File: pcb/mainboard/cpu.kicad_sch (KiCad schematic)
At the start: 25 parts, among them SW101 EVQPUJ02K, SW102 DNP, U100 MCIMX6Y7DVM09AB, Y101 24MHz, Y102 32.768kHz

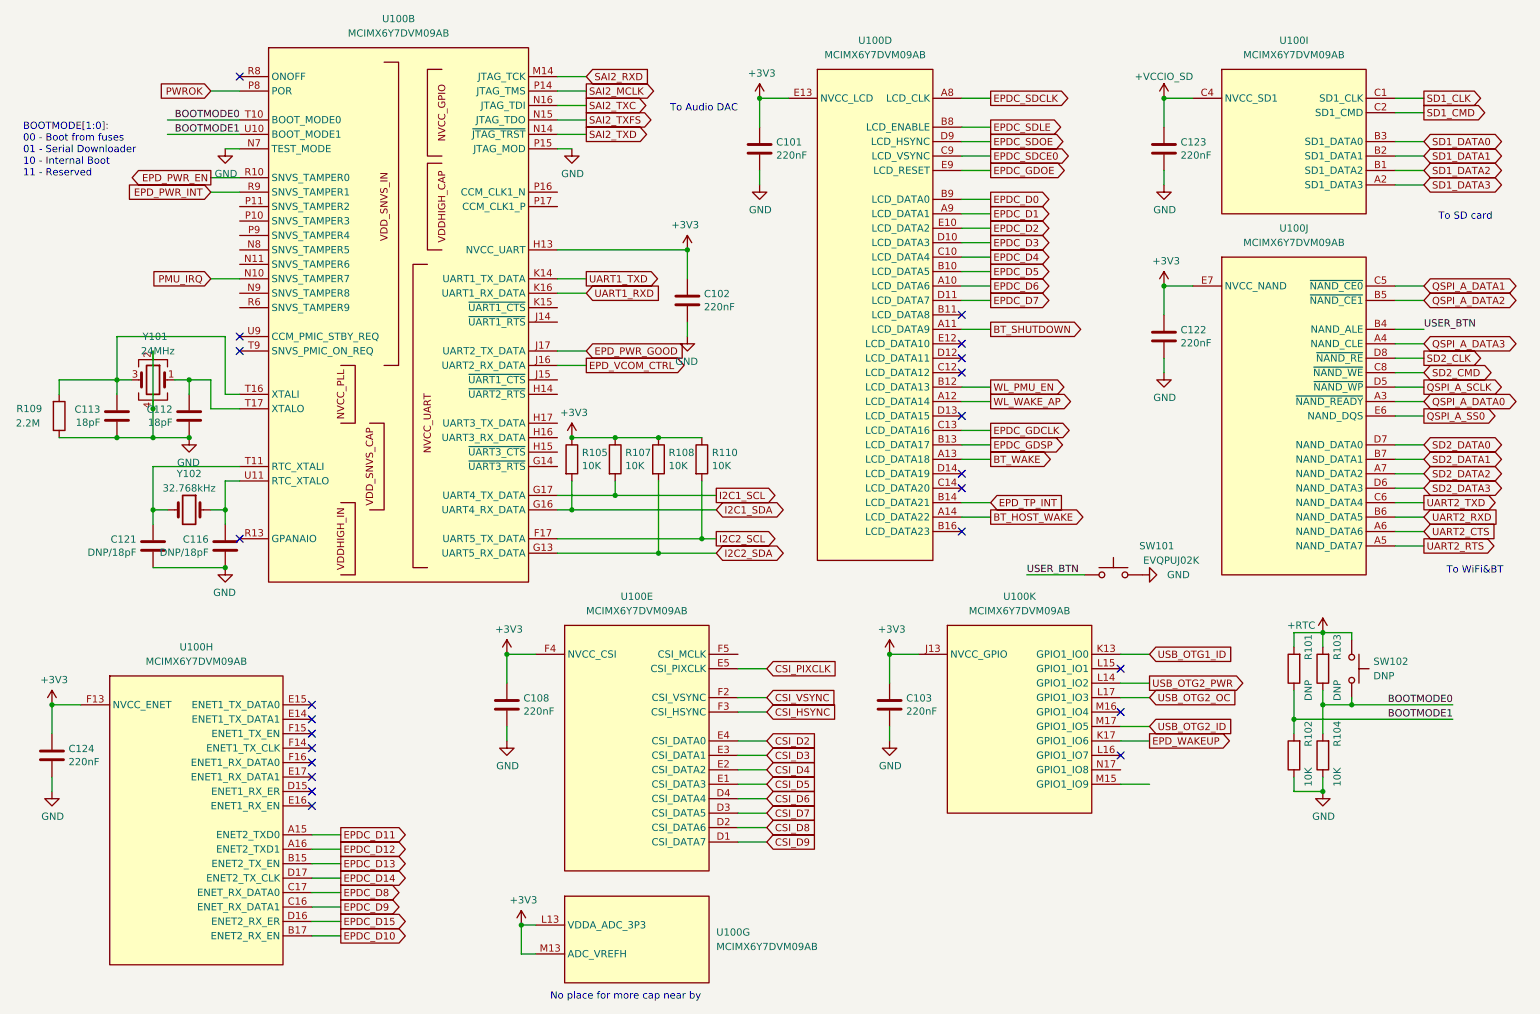
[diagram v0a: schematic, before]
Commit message: pcb: switch to max17135, length tuning for QSPI and SD
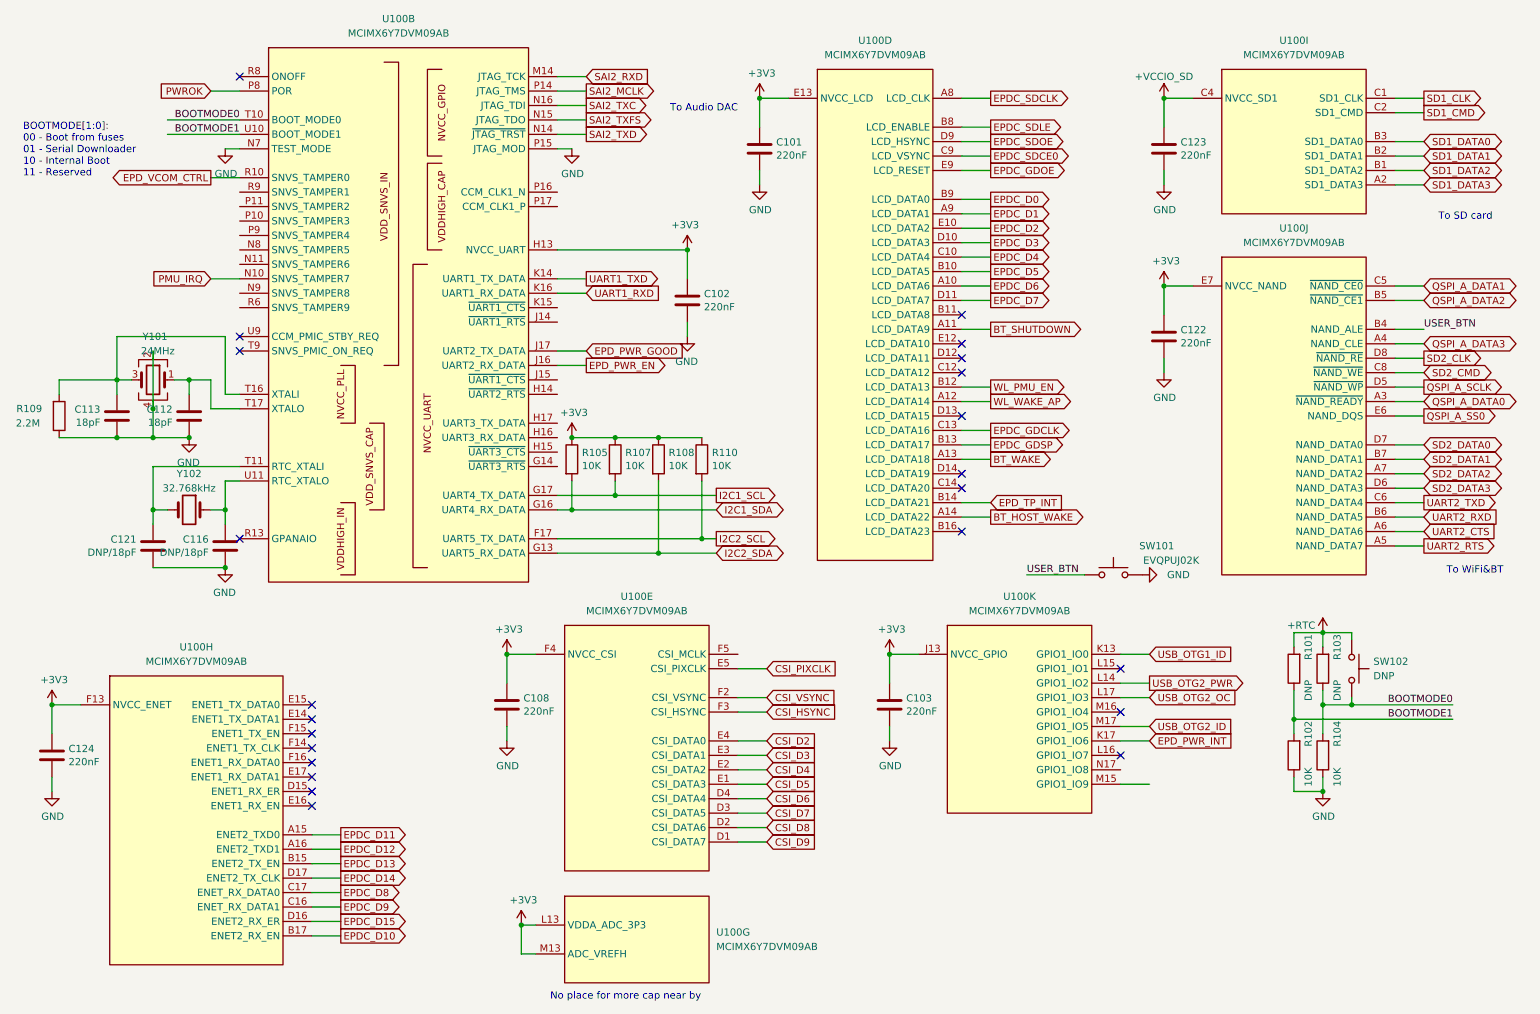
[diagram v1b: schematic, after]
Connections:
- net EPD_WAKEUP is gone; now on net EPD_PWR_INT: U100.K17 (GPIO1_IO6)
- net EPD_PWR_EN: now also U100.J16 (UART2_RX_DATA); no longer U100.R10 (SNVS_TAMPER0)
- net EPD_PWR_INT: no longer U100.R9 (SNVS_TAMPER1)
- net EPD_VCOM_CTRL: now also U100.R10 (SNVS_TAMPER0); no longer U100.J16 (UART2_RX_DATA)
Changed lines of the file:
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@@
     (stroke (width 0) (type solid) (color 0 0 0 0))
-  )
-  (wire (pts (xy 50.8 52.07) (xy 55.88 52.07))
-    (stroke (width 0) (type default) (color 0 0 0 0))
   )
   (wire (pts (xy 50.8 85.09) (xy 46.99 85.09))
@@
     )
   )
-  (global_label "EPD_PWR_EN" (shape output) (at 50.8 49.53 180)
+  (global_label "EPD_VCOM_CTRL" (shape output) (at 50.8 49.53 180)
     (effects (font (size 1.27 1.27)) (justify right))
     (property "Intersheet References" "${INTERSHEET_REFS}" (id 0) (at -53.34 163.83 0)
       (effects (font (size 1.27 1.27)) (justify left) hide)
-    )
-  )
-  (global_label "EPD_PWR_INT" (shape input) (at 50.8 52.07 180)
-    (effects (font (size 1.27 1.27)) (justify right))
-    (property "Intersheet References" "${INTERSHEET_REFS}" (id 0) (at -53.34 -62.23 0)
-      (effects (font (size 1.27 1.27)) hide)
     )
   )
@@
     )
   )
-  (global_label "EPD_VCOM_CTRL" (shape output) (at 116.84 82.55 0)
+  (global_label "EPD_PWR_EN" (shape output) (at 116.84 82.55 0)
     (effects (font (size 1.27 1.27)) (justify left))
     (property "Intersheet References" "${INTERSHEET_REFS}" (id 0) (at 220.98 -31.75 0)
@@
     )
   )
-  (global_label "EPD_WAKEUP" (shape output) (at 215.9 148.59 0)
+  (global_label "EPD_PWR_INT" (shape input) (at 215.9 148.59 0)
     (effects (font (size 1.27 1.27)) (justify left))
     (property "Intersheet References" "${INTERSHEET_REFS}" (id 0) (at 320.04 262.89 0)
